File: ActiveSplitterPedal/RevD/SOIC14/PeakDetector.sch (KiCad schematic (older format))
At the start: 9 parts, among them U3 TL074

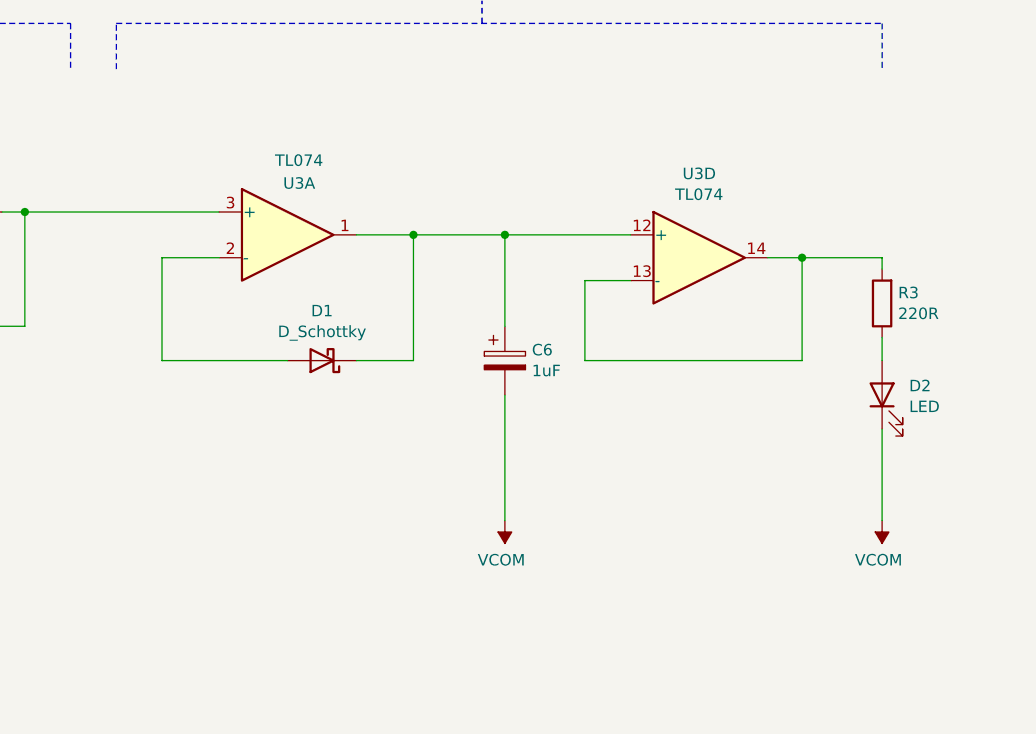
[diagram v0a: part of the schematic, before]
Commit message: fixed peak detector
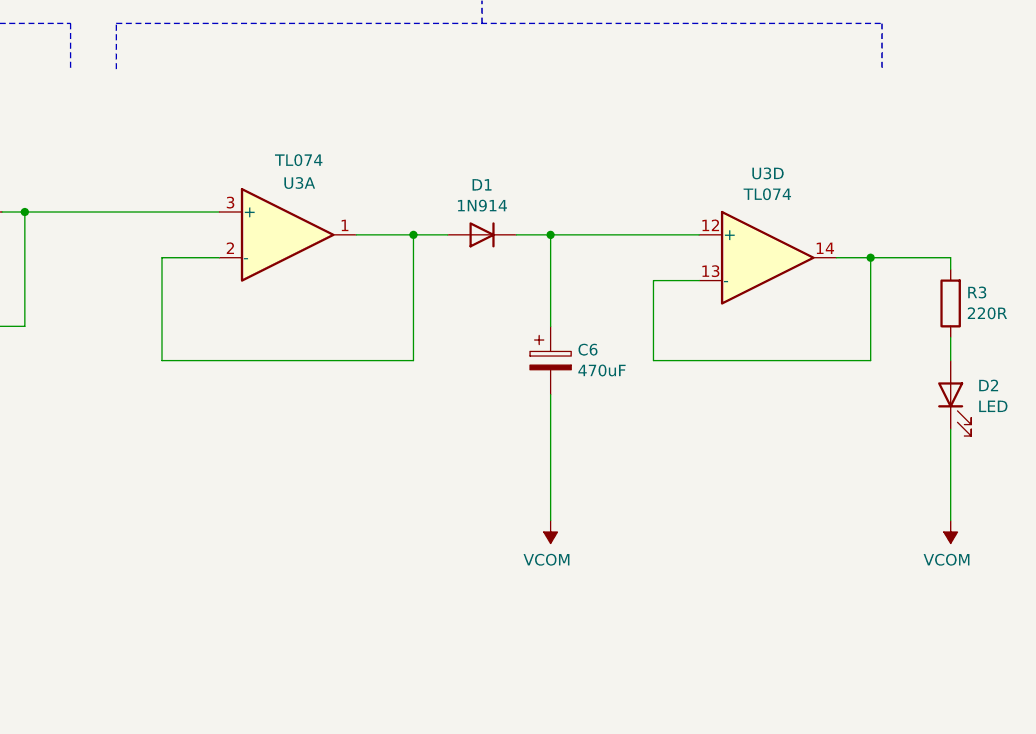
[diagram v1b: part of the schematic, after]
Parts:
- removed D1: D_Schottky, Diode_SMD:D_SOD-123F, symbol Device:D_Schottky
- added D1: 1N914, Diode_SMD:D_SOD-123F, symbol Device:D
- C6: value 1uF -> 470uF
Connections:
- net at C6.1, U3.12 (+): now also D1.1 (K); no longer U3.1
- net at U3.2 (-): now also U3.1, D1.2 (A)
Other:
- moved on the sheet: C6, D2, R3, U3D
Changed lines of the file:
@@
 L Amplifier_Operational:TL074 U3
 U 4 1 5F3F8AC2
-P 7400 2725
+P 7700 2725
 AR Path="/5F3F1F31/5F3F8AC2" Ref="U3"  Part="4"
 AR Path="/5F512144/5F3F8AC2" Ref="U?"  Part="4"
@@
 AR Path="/5F6A4453/5F3F8AC2" Ref="U9"  Part="4"
 AR Path="/5F6AEF1B/5F3F8AC2" Ref="U12"  Part="4"
-F 0 "U3" H 7400 3092 50  0000 C CNN
-F 1 "TL074" H 7400 3001 50  0000 C CNN
-F 2 "Package_SO:SOIC-14_3.9x8.7mm_P1.27mm" H 7350 2825 50  0001 C CNN
-F 3 "http://www.ti.com/lit/ds/symlink/tl071.pdf" H 7450 2925 50  0001 C CNN
-	4    7400 2725
+F 0 "U3" H 7700 3092 50  0000 C CNN
+F 1 "TL074" H 7700 3001 50  0000 C CNN
+F 2 "Package_SO:SOIC-14_3.9x8.7mm_P1.27mm" H 7650 2825 50  0001 C CNN
+F 3 "http://www.ti.com/lit/ds/symlink/tl071.pdf" H 7750 2925 50  0001 C CNN
+	4    7700 2725
 	1    0    0    -1
 $EndComp
@@
 	5050 2725 5050 3175
 Wire Wire Line
-	5050 3175 5600 3175
-Wire Wire Line
 	6150 3175 6150 2625
 Connection ~ 6150 2625
 Wire Wire Line
-	6550 3025 6550 2625
-Wire Wire Line
-	6550 3325 6550 3875
-Wire Wire Line
-	7100 2625 6550 2625
-Connection ~ 6550 2625
-Wire Wire Line
-	7100 2825 6900 2825
-Wire Wire Line
-	6900 2825 6900 3175
-Wire Wire Line
-	6900 3175 7850 3175
-Wire Wire Line
-	7850 3175 7850 2725
-Wire Wire Line
-	7850 2725 7700 2725
+	6750 3025 6750 2625
+Connection ~ 6750 2625
+Wire Wire Line
+	7400 2825 7200 2825
+Wire Wire Line
+	7200 2825 7200 3175
+Wire Wire Line
+	7200 3175 8150 3175
+Wire Wire Line
+	8150 3175 8150 2725
+Wire Wire Line
+	8150 2725 8000 2725
 $Comp
 L Device:C C5
@@
 L Device:LED D2
 U 1 1 5F4B9375
-P 8200 3325
+P 8500 3325
 AR Path="/5F3F1F31/5F4B9375" Ref="D2"  Part="1"
 AR Path="/5F512144/5F4B9375" Ref="D?"  Part="1"
@@
 AR Path="/5F6A4453/5F4B9375" Ref="D6"  Part="1"
 AR Path="/5F6AEF1B/5F4B9375" Ref="D8"  Part="1"
-F 0 "D2" V 8239 3207 50  0000 R CNN
-F 1 "LED" V 8148 3207 50  0000 R CNN
-F 2 "LED_THT:LED_D5.0mm" H 8200 3325 50  0001 C CNN
-F 3 "~" H 8200 3325 50  0001 C CNN
-	1    8200 3325
+F 0 "D2" V 8539 3207 50  0000 R CNN
+F 1 "LED" V 8448 3207 50  0000 R CNN
+F 2 "LED_THT:LED_D5.0mm" H 8500 3325 50  0001 C CNN
+F 3 "~" H 8500 3325 50  0001 C CNN
+	1    8500 3325
 	0    -1   -1   0
 $EndComp
 Wire Wire Line
-	8200 3175 8200 3075
-Wire Wire Line
-	8200 2725 7850 2725
-Connection ~ 7850 2725
-Wire Wire Line
-	8200 3475 8200 3875
-$Comp
-L Device:D_Schottky D1
-U 1 1 5F3FDBB2
-P 5750 3175
-AR Path="/5F3F1F31/5F3FDBB2" Ref="D1"  Part="1"
-AR Path="/5F512144/5F3FDBB2" Ref="D?"  Part="1"
-AR Path="/5F515E89/5F3FDBB2" Ref="D?"  Part="1"
-AR Path="/5F519B24/5F3FDBB2" Ref="D?"  Part="1"
-AR Path="/5F6A30A9/5F3FDBB2" Ref="D3"  Part="1"
-AR Path="/5F6A4453/5F3FDBB2" Ref="D5"  Part="1"
-AR Path="/5F6AEF1B/5F3FDBB2" Ref="D7"  Part="1"
-F 0 "D1" H 5750 2958 50  0000 C CNN
-F 1 "D_Schottky" H 5750 3049 50  0000 C CNN
-F 2 "Diode_SMD:D_SOD-123F" H 5750 3175 50  0001 C CNN
-F 3 "~" H 5750 3175 50  0001 C CNN
-	1    5750 3175
-	-1   0    0    1
-$EndComp
+	8500 3175 8500 3075
+Wire Wire Line
+	8500 2725 8150 2725
+Connection ~ 8150 2725
+Wire Wire Line
+	8500 3475 8500 3875
 Connection ~ 2600 5600
 Wire Wire Line
@@
 L Device:R R3
 U 1 1 5F579AC3
-P 8200 2925
+P 8500 2925
 AR Path="/5F3F1F31/5F579AC3" Ref="R3"  Part="1"
 AR Path="/5F512144/5F579AC3" Ref="R?"  Part="1"
@@
 AR Path="/5F6A4453/5F579AC3" Ref="R15"  Part="1"
 AR Path="/5F6AEF1B/5F579AC3" Ref="R21"  Part="1"
-F 0 "R3" H 8130 2879 50  0000 R CNN
-F 1 "220R" H 8130 2970 50  0000 R CNN
-F 2 "Resistor_SMD:R_0805_2012Metric_Pad1.15x1.40mm_HandSolder" V 8130 2925 50  0001 C CNN
-F 3 "~" H 8200 2925 50  0001 C CNN
-	1    8200 2925
-	-1   0    0    1
-$EndComp
-Wire Wire Line
-	8200 2775 8200 2725
-Wire Wire Line
-	6150 2625 6550 2625
-Wire Wire Line
-	5900 3175 6150 3175
+F 0 "R3" H 8430 2879 50  0000 R CNN
+F 1 "220R" H 8430 2970 50  0000 R CNN
+F 2 "Resistor_SMD:R_0805_2012Metric_Pad1.15x1.40mm_HandSolder" V 8430 2925 50  0001 C CNN
+F 3 "~" H 8500 2925 50  0001 C CNN
+	1    8500 2925
+	-1   0    0    1
+$EndComp
+Wire Wire Line
+	8500 2775 8500 2725
 Wire Wire Line
 	5900 2625 6150 2625
@@
 L Device:CP C6
 U 1 1 5F5AD5B8
-P 6550 3175
+P 6750 3175
 AR Path="/5F3F1F31/5F5AD5B8" Ref="C6"  Part="1"
 AR Path="/5F519B24/5F5AD5B8" Ref="C?"  Part="1"
@@
 AR Path="/5F6A4453/5F5AD5B8" Ref="C28"  Part="1"
 AR Path="/5F6AEF1B/5F5AD5B8" Ref="C39"  Part="1"
-F 0 "C6" H 6668 3221 50  0000 L CNN
-F 1 "1uF" H 6668 3130 50  0000 L CNN
-F 2 "Capacitor_SMD:C_Elec_4x5.8" H 6588 3025 50  0001 C CNN
-F 3 "~" H 6550 3175 50  0001 C CNN
-	1    6550 3175
+F 0 "C6" H 6868 3221 50  0000 L CNN
+F 1 "470uF" H 6868 3130 50  0000 L CNN
+F 2 "Capacitor_SMD:C_Elec_4x5.8" H 6788 3025 50  0001 C CNN
+F 3 "~" H 6750 3175 50  0001 C CNN
+	1    6750 3175
 	1    0    0    -1
 $EndComp
@@
 L power:VCOM #PWR0106
 U 1 1 5F59A32D
-P 6550 3875
+P 6750 3875
 AR Path="/5F3F1F31/5F59A32D" Ref="#PWR0106"  Part="1"
 AR Path="/5F6A30A9/5F59A32D" Ref="#PWR0118"  Part="1"
 AR Path="/5F6A4453/5F59A32D" Ref="#PWR0130"  Part="1"
 AR Path="/5F6AEF1B/5F59A32D" Ref="#PWR0142"  Part="1"
-F 0 "#PWR0106" H 6550 3725 50  0001 C CNN
-F 1 "VCOM" H 6565 4048 50  0000 C CNN
-F 2 "" H 6550 3875 50  0001 C CNN
-F 3 "" H 6550 3875 50  0001 C CNN
-	1    6550 3875
+F 0 "#PWR0106" H 6750 3725 50  0001 C CNN
+F 1 "VCOM" H 6765 4048 50  0000 C CNN
+F 2 "" H 6750 3875 50  0001 C CNN
+F 3 "" H 6750 3875 50  0001 C CNN
+	1    6750 3875
 	-1   0    0    1
 $EndComp
@@
 L power:VCOM #PWR0107
 U 1 1 5F59A89E
-P 8200 3875
+P 8500 3875
 AR Path="/5F3F1F31/5F59A89E" Ref="#PWR0107"  Part="1"
 AR Path="/5F6A30A9/5F59A89E" Ref="#PWR0119"  Part="1"
 AR Path="/5F6A4453/5F59A89E" Ref="#PWR0131"  Part="1"
 AR Path="/5F6AEF1B/5F59A89E" Ref="#PWR0143"  Part="1"
-F 0 "#PWR0107" H 8200 3725 50  0001 C CNN
-F 1 "VCOM" H 8215 4048 50  0000 C CNN
-F 2 "" H 8200 3875 50  0001 C CNN
-F 3 "" H 8200 3875 50  0001 C CNN
-	1    8200 3875
+F 0 "#PWR0107" H 8500 3725 50  0001 C CNN
+F 1 "VCOM" H 8515 4048 50  0000 C CNN
+F 2 "" H 8500 3875 50  0001 C CNN
+F 3 "" H 8500 3875 50  0001 C CNN
+	1    8500 3875
 	-1   0    0    1
 $EndComp
@@
 	-1   0    0    1
 $EndComp
+Wire Wire Line
+	6150 2625 6300 2625
+Wire Wire Line
+	6600 2625 6750 2625
+Wire Wire Line
+	5050 3175 6150 3175
+Wire Wire Line
+	6750 2625 7400 2625
+Wire Wire Line
+	6750 3325 6750 3875
+$Comp
+L Device:D D1
+U 1 1 5F60D8BF
+P 6450 2625
+AR Path="/5F3F1F31/5F60D8BF" Ref="D1"  Part="1"
+AR Path="/5F6A30A9/5F60D8BF" Ref="D3"  Part="1"
+AR Path="/5F6A4453/5F60D8BF" Ref="D5"  Part="1"
+AR Path="/5F6AEF1B/5F60D8BF" Ref="D7"  Part="1"
+F 0 "D1" H 6450 2408 50  0000 C CNN
+F 1 "1N914" H 6450 2499 50  0000 C CNN
+F 2 "Diode_SMD:D_SOD-123F" H 6450 2625 50  0001 C CNN
+F 3 "~" H 6450 2625 50  0001 C CNN
+	1    6450 2625
+	-1   0    0    1
+$EndComp

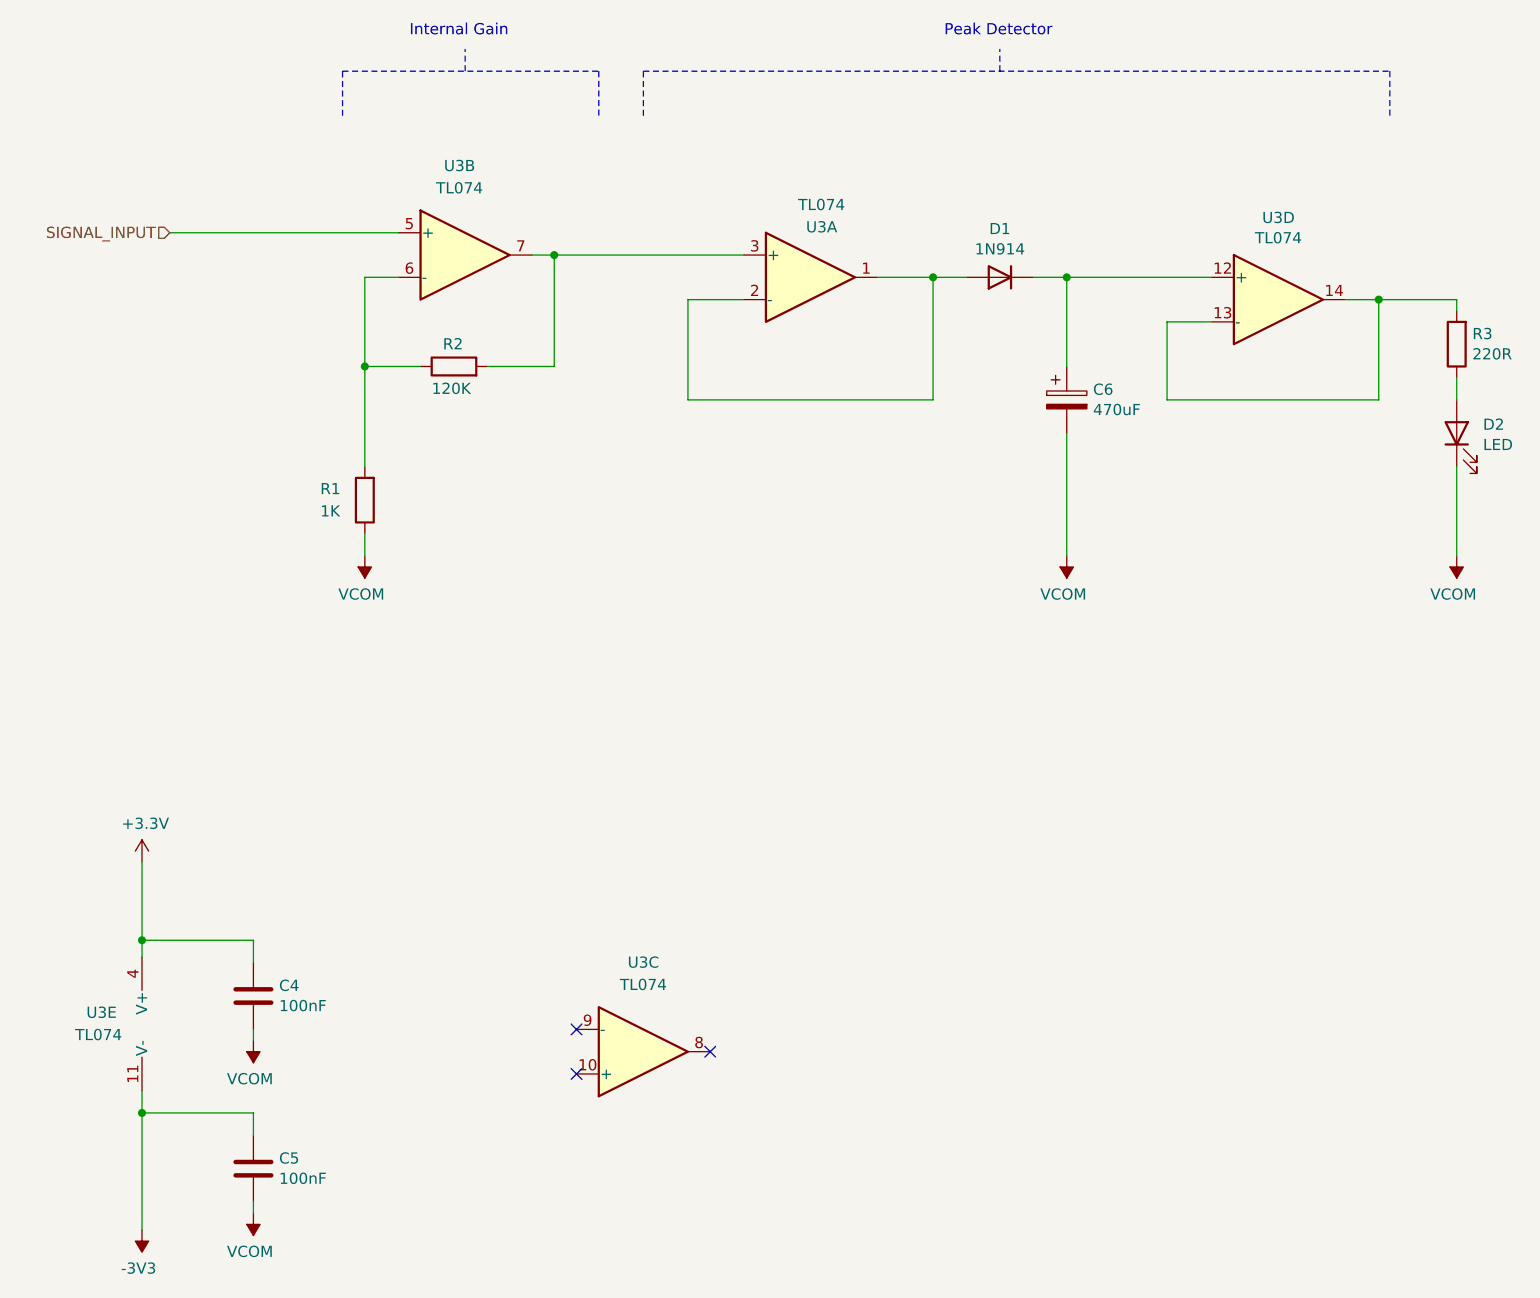
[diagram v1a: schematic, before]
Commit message: updated layout
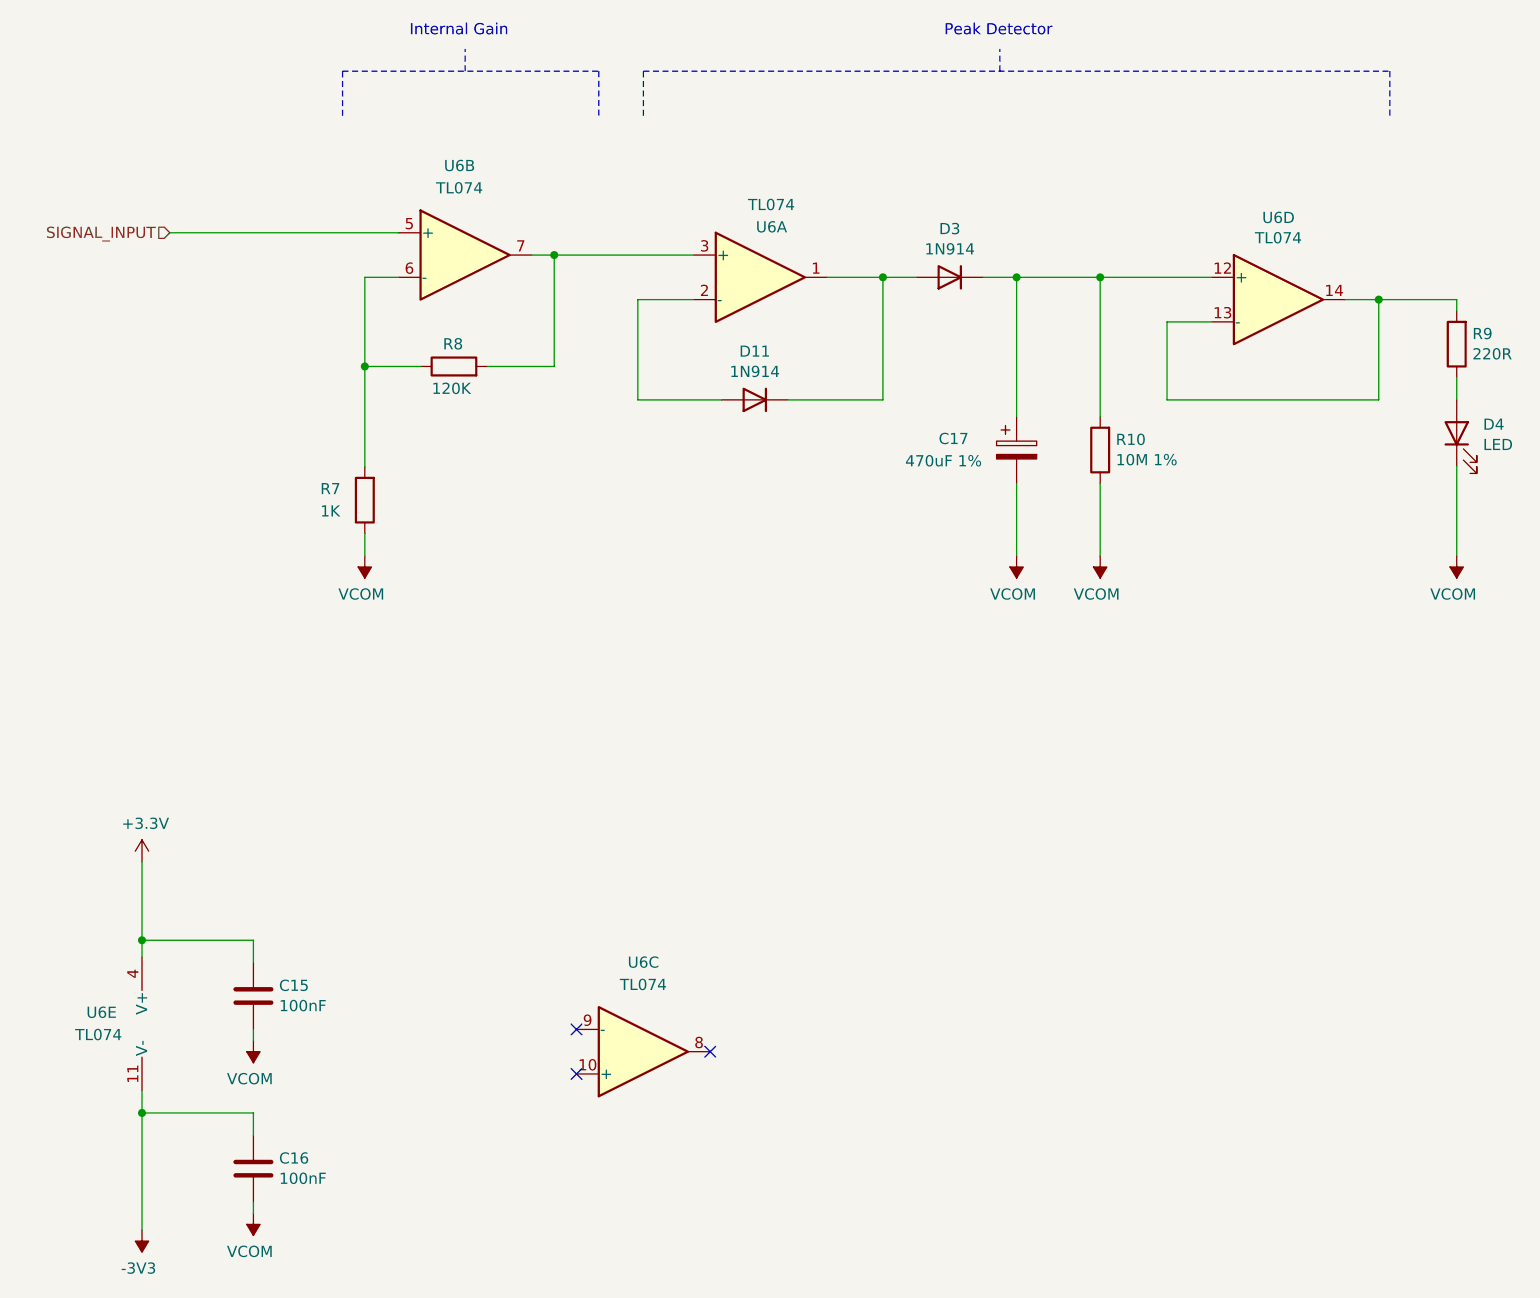
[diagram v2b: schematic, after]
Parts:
- added D10: 1N914, Diode_SMD:D_SOD-123F, symbol Device:D
- added R4: 10M 1%, Resistor_SMD:R_0805_2012Metric_Pad1.15x1.40mm_HandSolder, symbol Device:R
- C6: value 470uF -> 470uF 1%; footprint Capacitor_SMD:C_Elec_4x5.8 -> Capacitor_SMD:C_1210_3225Metric_Pad1.42x2.65mm_HandSolder
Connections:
- net VCOM: now also R4.1
- net at D1.2 (A), U3.1: now also D10.1 (K); no longer U3.2 (-)
- net at C6.1, D1.1 (K), U3.12 (+): now also R4.2
- new net: D10.2 (A), U3.2 (-)
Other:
- moved on the sheet: C17, D3, U6A
